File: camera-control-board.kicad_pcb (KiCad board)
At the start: 6 copper layers, 90 x 96 mm, 51 parts, among them J1 DF12NB-36DS-0.5V_51_, J2 10104110-0001LF, J3 104031-0811, J4 02x05 M 1.27mm, J5 Conn_01x09, SW1 CAS-120TA, SW3 SW_Push, U1 STM32H743IITx, U2 IS42S32800J-7TLI, U3 W25Q256JVEIQ TR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

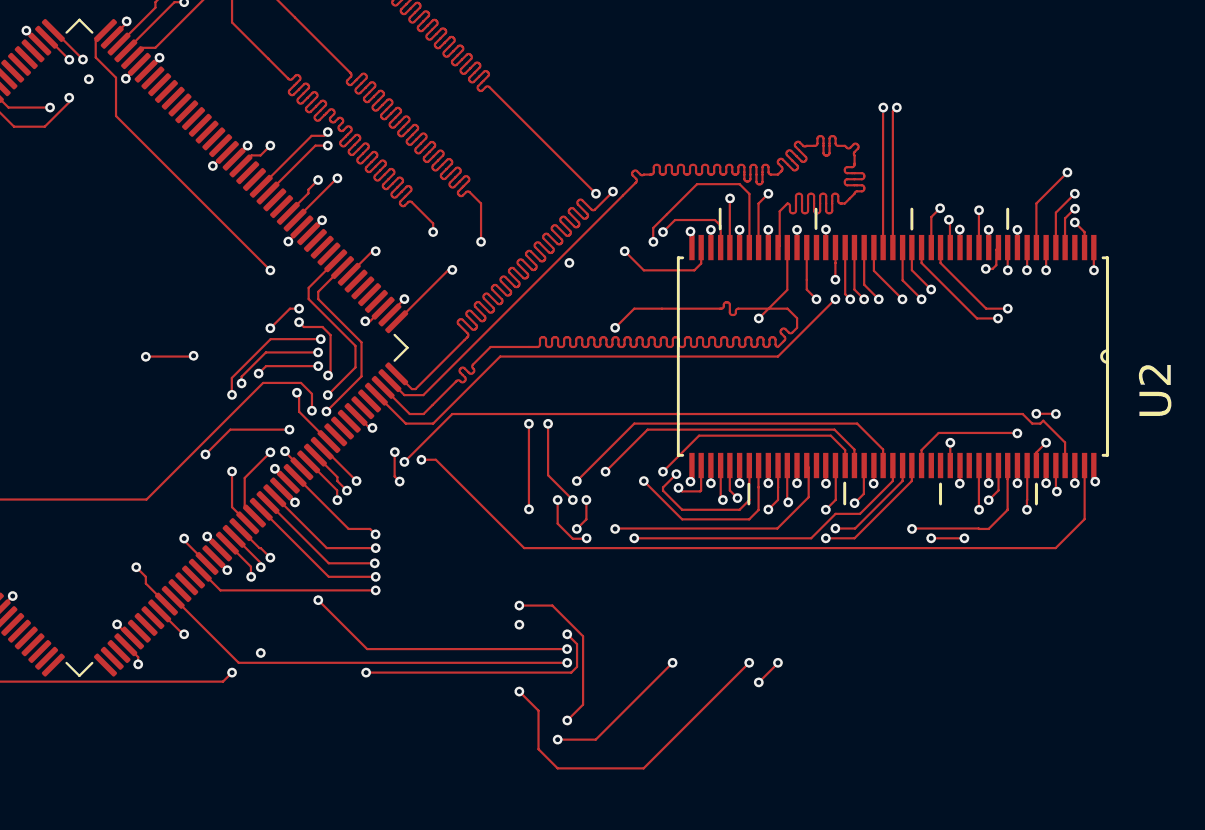
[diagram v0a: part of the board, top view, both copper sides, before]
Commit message: all SDRAM traces laid out and length matched.
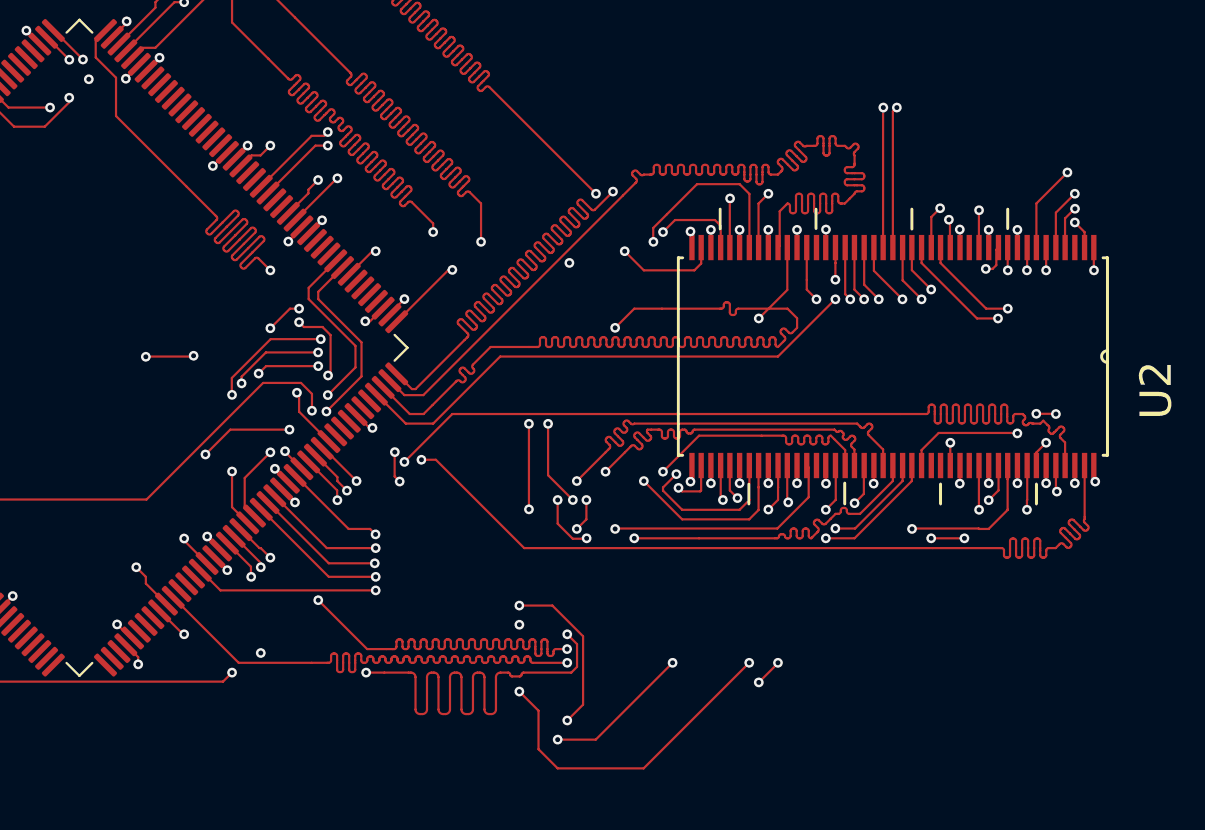
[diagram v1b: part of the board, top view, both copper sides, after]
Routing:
- net /DRAM_D27: track 58.0 -> 80.4 mm
- net /DRAM_A9: track 41.6 -> 63.4 mm
- net /DRAM_CLKE: track 44.7 -> 65.0 mm
- net /DRAM_D26: track 47.8 -> 66.5 mm
- net /DRAM_A8: track 45.0 -> 63.7 mm
- net /DRAM_D24: track 47.2 -> 65.4 mm
- net /DRAM_D11: track 47.5 -> 64.6 mm
- net /DRAM_D10: track 47.3 -> 63.7 mm
- net /DRAM_D25: track 49.1 -> 65.3 mm
- net /DRAM_A6: track 49.3 -> 63.8 mm
- net /DRAM_D14: track 52.4 -> 65.7 mm
- net /DRAM_D8: track 52.8 -> 65.3 mm
- net /DRAM_D9: track 53.4 -> 63.8 mm
- net /DRAM_D15: track 55.5 -> 65.8 mm
- net /DRAM_D13: track 55.5 -> 65.6 mm
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
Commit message: All SDRAM traces complete.
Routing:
- net GND: track 25.5 -> 189.1 mm

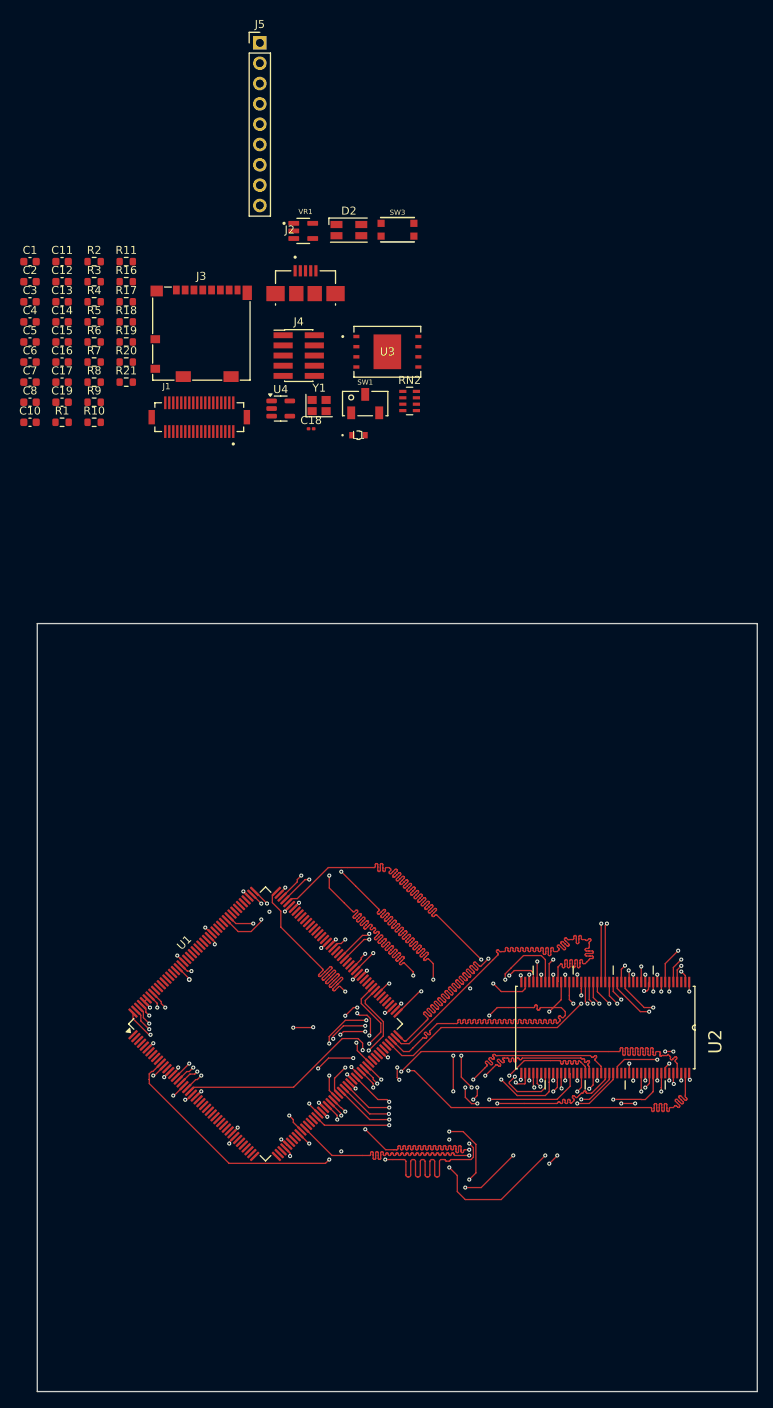
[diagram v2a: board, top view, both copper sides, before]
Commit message: added USB C connection
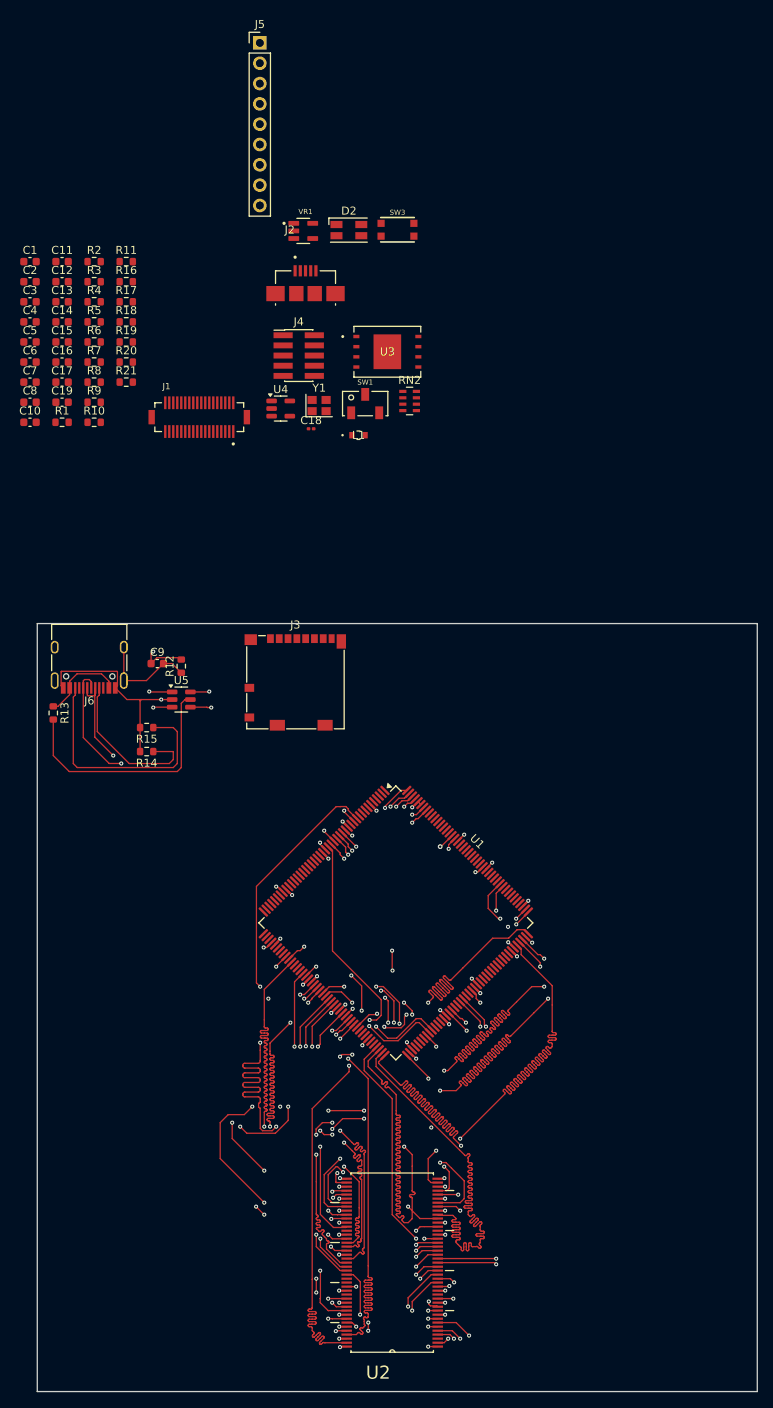
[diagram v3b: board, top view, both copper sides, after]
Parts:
- added C9: 4.7nF, Capacitor_SMD:C_0603_1608Metric, F.Cu at (47.5, 100.5)
- added J6: USB_C_Receptacle_USB2.0, Connector_USB:USB_C_Receptacle_HRO_TYPE-C-31-M-12, F.Cu at (39.0, 99.5)
- added R12: 1M, Resistor_SMD:R_0603_1608Metric, F.Cu at (50.5, 100.8)
- added R13: 0R, Resistor_SMD:R_0603_1608Metric, F.Cu at (34.5, 106.7)
- added R14: 5.1K, Resistor_SMD:R_0603_1608Metric, F.Cu at (46.2, 111.5)
- added R15: 5.1K, Resistor_SMD:R_0603_1608Metric, F.Cu at (46.2, 108.5)
- added U5: WE-TVS-82400102, Package_TO_SOT_SMD:SOT-23-6, F.Cu at (50.5, 105.0)
- moved J3 45.1 mm to (64.8, 102.8)
- moved U2 39.7 mm to (76.9, 175.4), turned to 180 degrees
- moved U1 20.6 mm to (77.3, 132.9), turned to -45 degrees
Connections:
- U1 pad 122: /FS_DM -> /ES_D-
- U1 pad 123: /FS_DP -> /ES_D+
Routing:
- net GND: track 189.1 -> 263.8 mm, vias 25 -> 27
- net /D+: track 0.00 -> 39.7 mm, vias 0 -> 2
- net /D-: track 0.00 -> 33.6 mm, vias 0 -> 2
- net VBUS: track 0.00 -> 30.9 mm
- net Net-(J6-CC2): track 0.00 -> 30.2 mm
- net Net-(J6-CC1): track 0.00 -> 20.4 mm
- net Net-(J6-SHIELD): track 0.00 -> 12.7 mm
- net Net-(J6-VBUS-PadA4): track 0.00 -> 10.8 mm
- net /ES_D+: track 0.00 -> 2.88 mm, vias 0 -> 1
- net /ES_D-: track 0.00 -> 2.38 mm, vias 0 -> 1

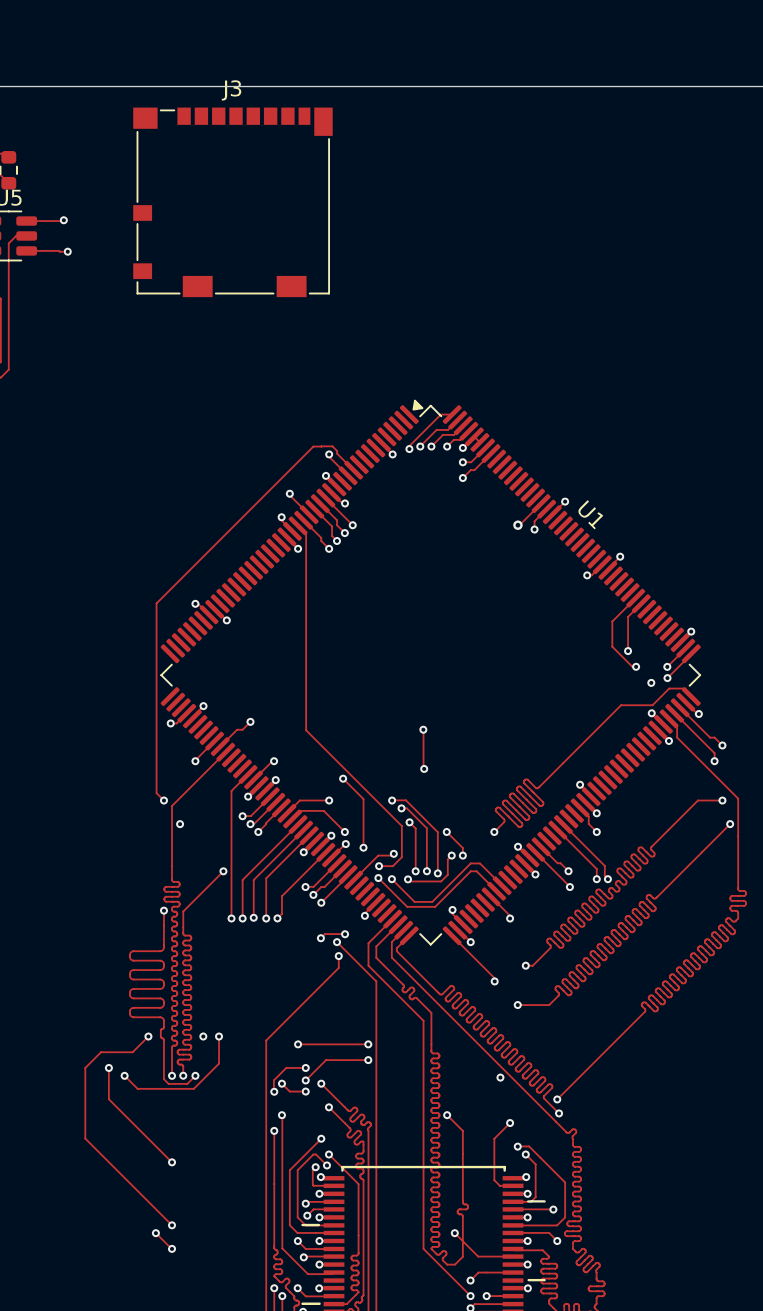
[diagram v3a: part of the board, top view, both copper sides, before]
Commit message: shhh fixed lowkey wrong trace sizes
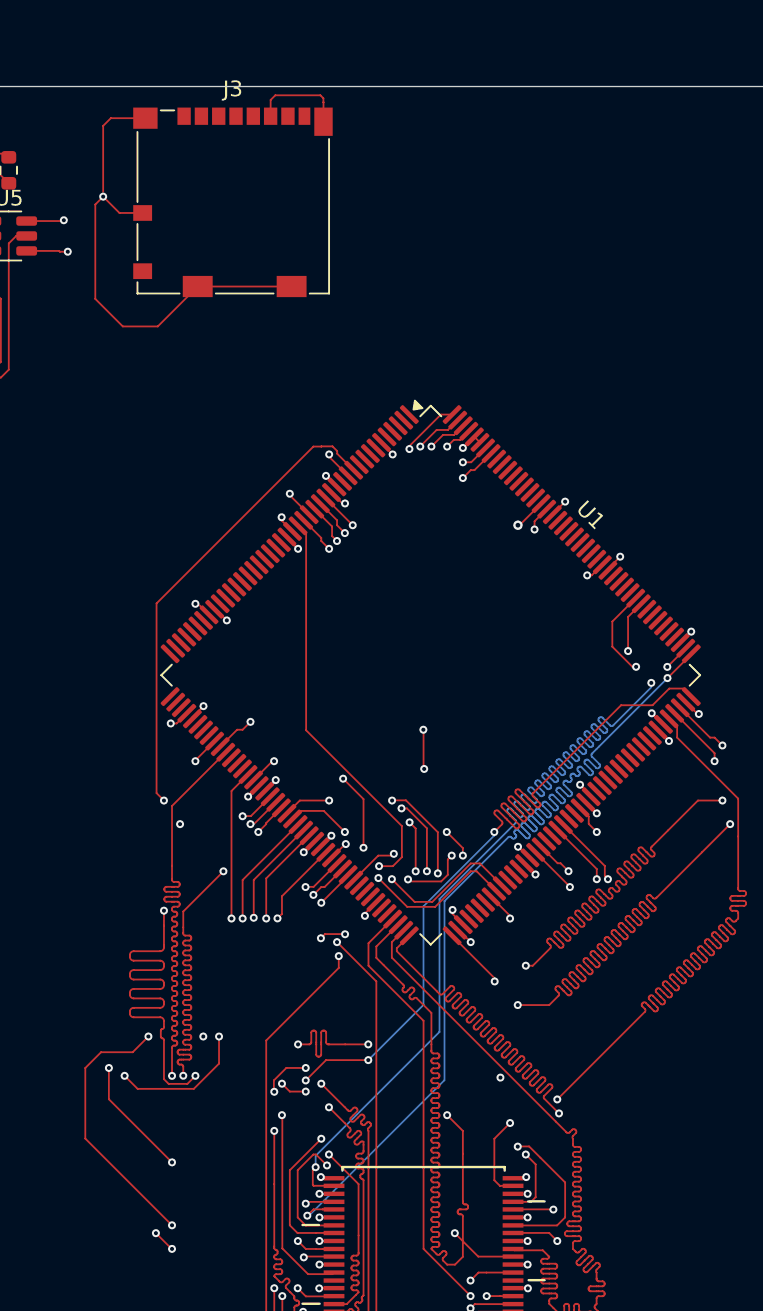
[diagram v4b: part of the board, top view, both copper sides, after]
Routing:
- net GND: track 263.8 -> 308.5 mm, vias 27 -> 28
- net /DRAM_D27: track 80.4 -> 62.5 mm
- net /DRAM_D11: track 64.6 -> 71.5 mm
- net /DRAM_D24: track 65.4 -> 70.7 mm
- net /DRAM_D25: track 65.3 -> 62.5 mm
- net /DRAM_D26: track 66.5 -> 64.0 mm

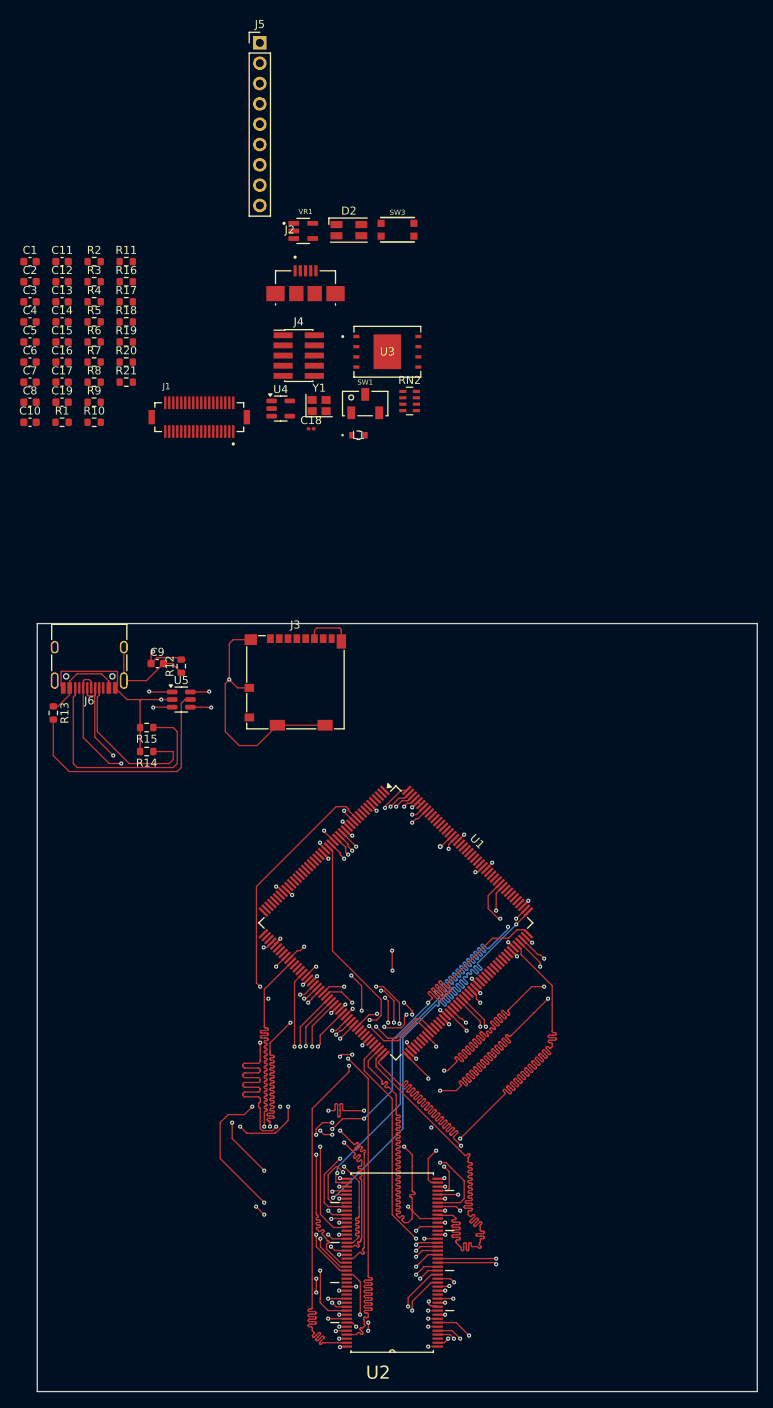
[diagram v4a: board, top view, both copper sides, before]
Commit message: SD Card routed (theoretically), now adding connector.
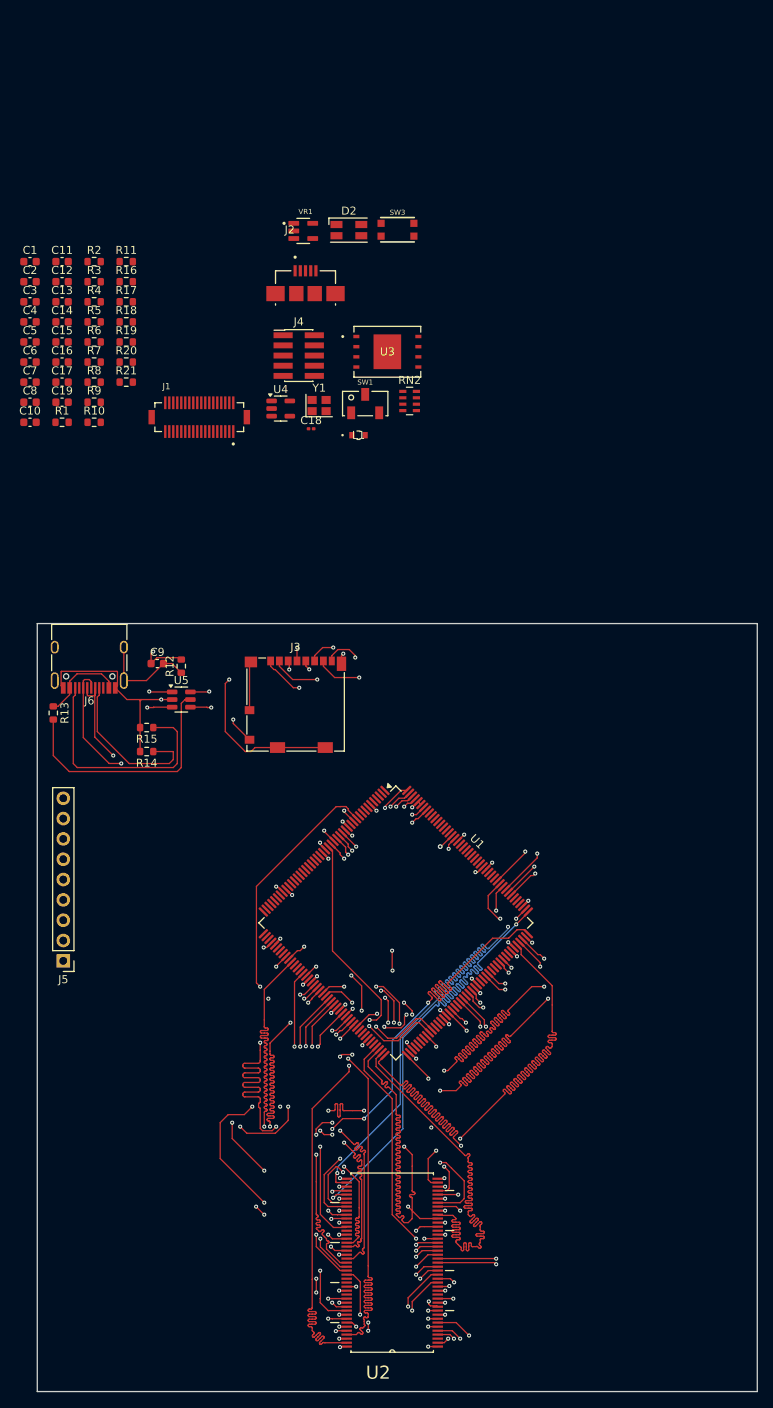
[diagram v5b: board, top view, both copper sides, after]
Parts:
- moved J5 117.3 mm to (35.8, 137.7), turned to 180 degrees
- moved J3 2.79 mm to (64.8, 105.6)
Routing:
- net /SD_CD: track 0.00 -> 121.2 mm, vias 0 -> 2
- net /ES_D-: track 2.38 -> 99.1 mm, vias 1 -> 2
- net /ES_D+: track 2.88 -> 93.0 mm, vias 1 -> 2
- net /SDIO_D0: track 0.00 -> 73.0 mm, vias 0 -> 2
- net /SDIO_D1: track 0.00 -> 72.9 mm, vias 0 -> 2
- net +3.3V: track 177.5 -> 245.5 mm, vias 26 -> 27
- net /SDIO_D2: track 0.00 -> 48.6 mm, vias 0 -> 2
- net /SDIO_D3: track 0.00 -> 47.4 mm, vias 0 -> 2
- net /SDIO_CLK: track 0.00 -> 45.4 mm, vias 0 -> 2
- net /SDIO_CMD: track 0.00 -> 45.2 mm, vias 0 -> 2
- net GND: track 308.5 -> 322.4 mm, vias 28 -> 30

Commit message: Finished connector.
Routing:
- net /SPI2_NSS: track 0.00 -> 171.8 mm, vias 0 -> 1
- net /SPI2_MISO: track 0.00 -> 168.9 mm, vias 0 -> 5
- net /SPI2_MOSI: track 0.00 -> 165.9 mm, vias 0 -> 2
- net /SPI2_SCLK: track 0.00 -> 163.7 mm, vias 0 -> 2
- net /I2C2_SDA: track 0.00 -> 65.5 mm, vias 0 -> 2
- net /I2C2_SCL: track 0.00 -> 63.8 mm, vias 0 -> 1
